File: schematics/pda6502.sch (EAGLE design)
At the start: 25 parts, among them IC1 74HC00D, IC2 74HC138D, IC3 DS1813-SMD, U1 W65C02S, U2 W65C22S, U3 28C256, U4 UM61256AK-12

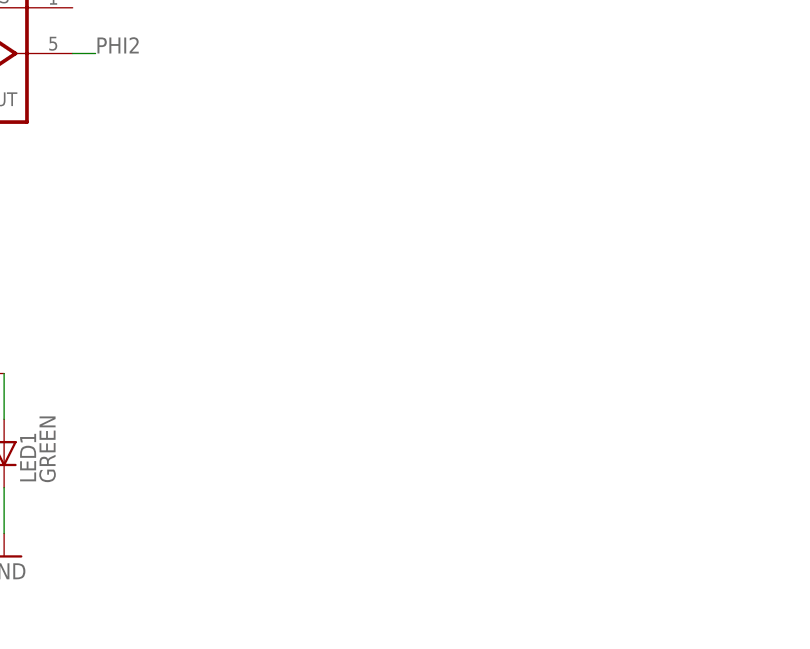
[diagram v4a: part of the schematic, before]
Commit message: schematics: VIA exposes two 2x7 headers; port A and port B.
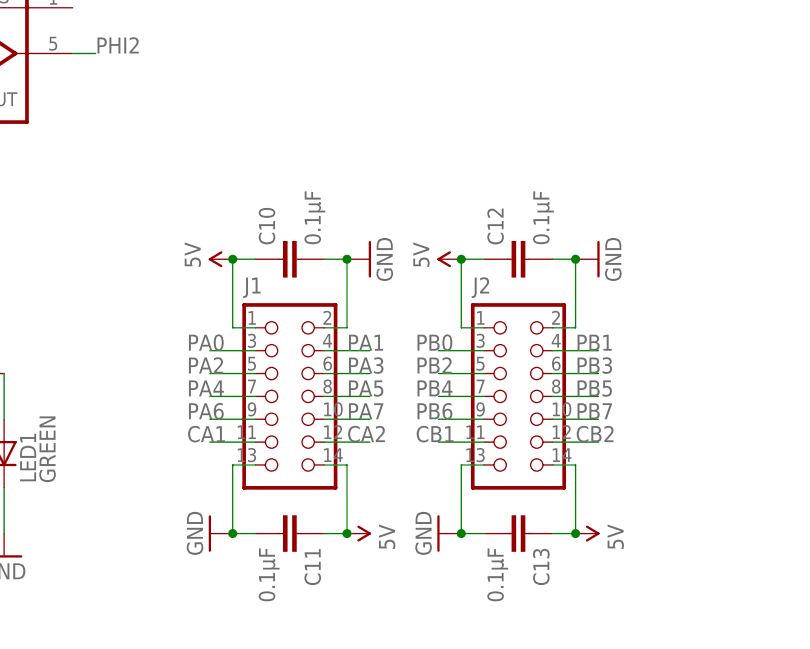
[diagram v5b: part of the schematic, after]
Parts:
- added C10, C11, C12, C13: 0.1μF, rcl:C-EUC0805
- added J1, J2: CON_HEADER_2X07-PTH, dangerousprototypes_devices:CON_HEADER_2X07-PTH
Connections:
- net 5V: now also C10.1, C11.1, C12.1, C13.1, J1.1, J1.14, J2.1, J2.14
- net CA1: now also J1.11
- net CA2: now also J1.12
- net CB1: now also J2.11
- net CB2: now also J2.12
- net GND: now also C10.2, C11.2, C12.2, C13.2, J1.13, J1.2, J2.13, J2.2
- net PA0: now also J1.3
- net PA1: now also J1.4
- net PA2: now also J1.5
- net PA3: now also J1.6
- net PA4: now also J1.7
- net PA5: now also J1.8
- net PA6: now also J1.9
- net PA7: now also J1.10
- net PB0: now also J2.3
- net PB1: now also J2.4
- net PB2: now also J2.5
- net PB3: now also J2.6
- net PB4: now also J2.7
- net PB5: now also J2.8
- net PB6: now also J2.9
- net PB7: now also J2.10

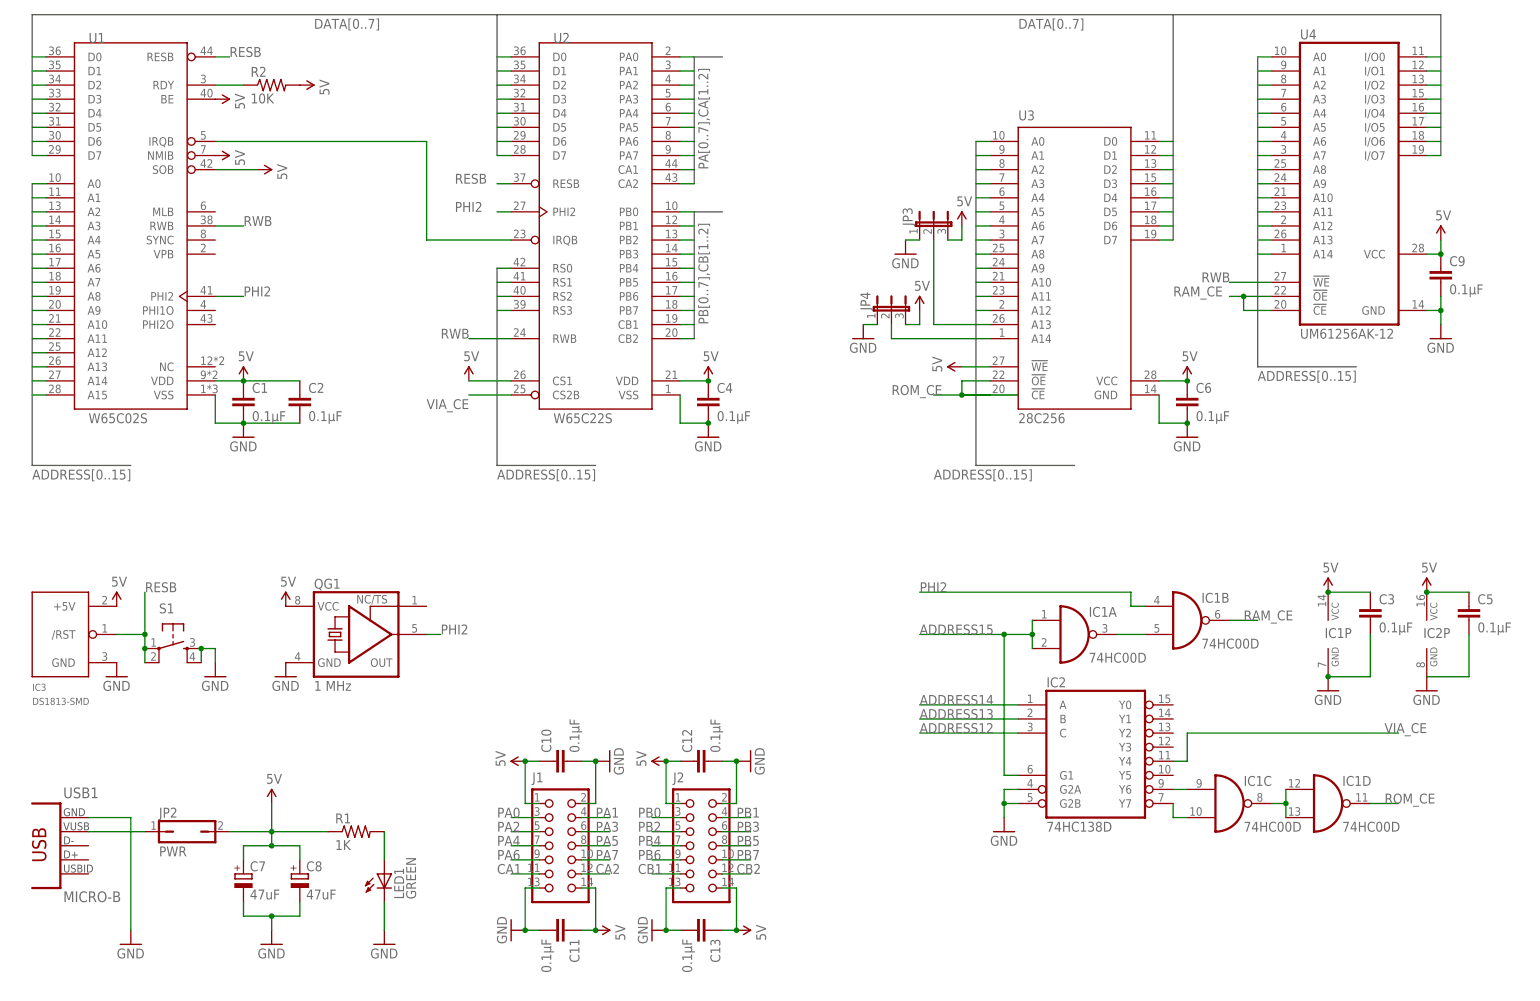
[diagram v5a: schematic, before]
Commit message: schematics: layout tweaks and errors corrected in schematic.
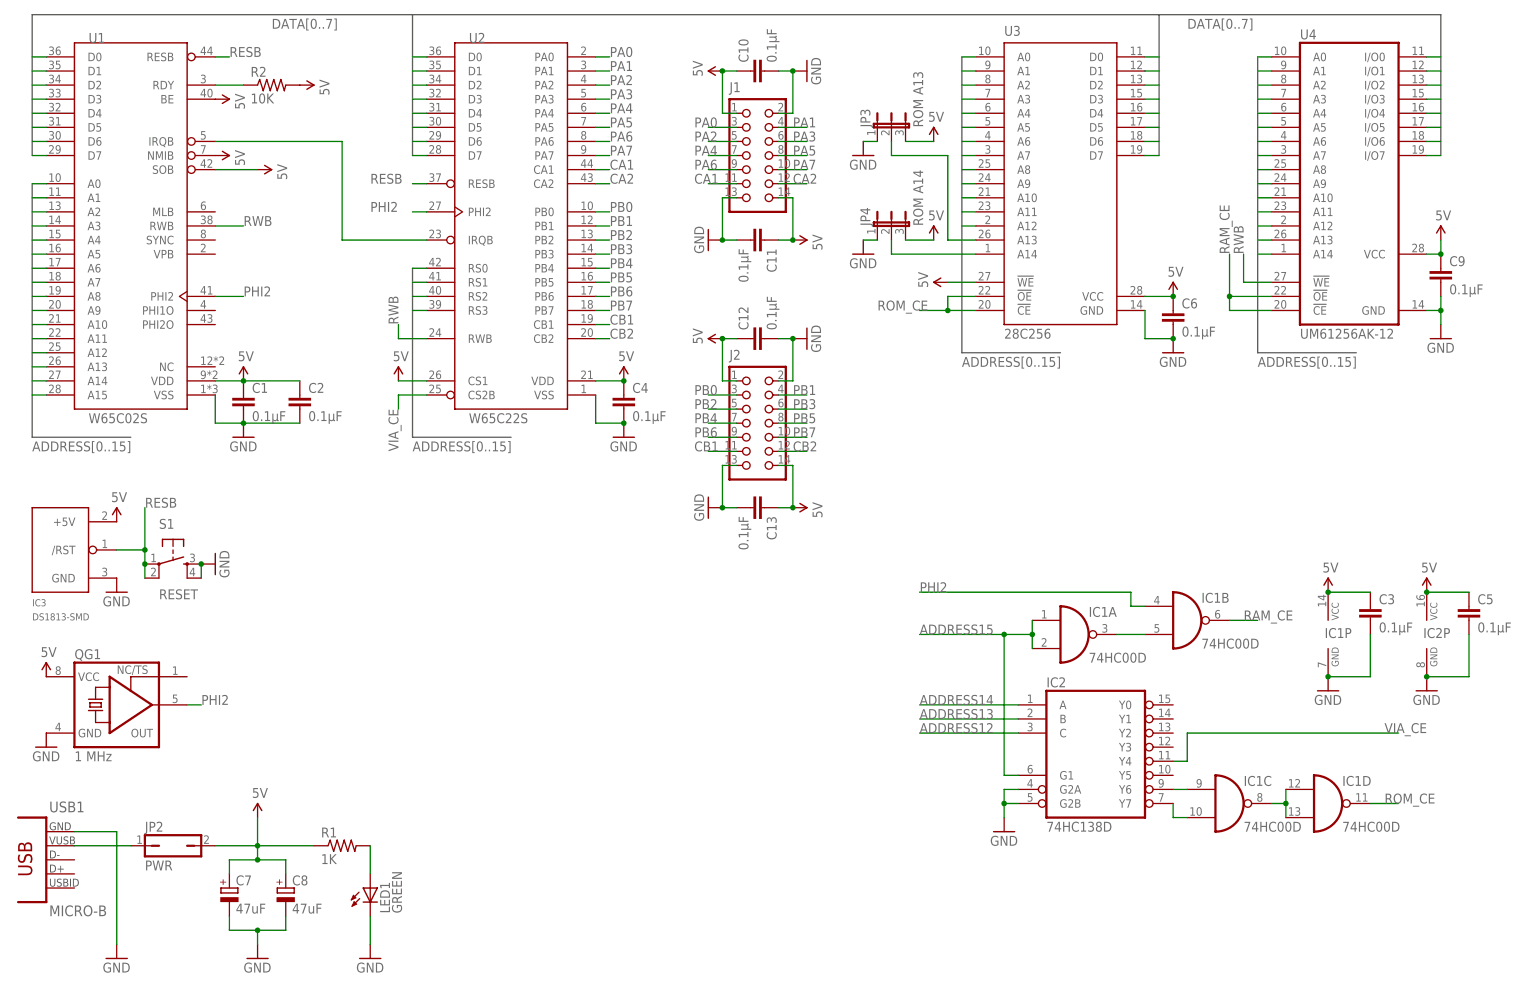
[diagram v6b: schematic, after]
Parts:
- JP3: value (none) -> ROM A13
- JP4: value (none) -> ROM A14
- S1: value (none) -> RESET
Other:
- moved on the sheet: C10, C11, C12, C13, C4, C6, C7, C8, IC3, J1, J2, JP2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

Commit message: schematics: TFT+SD header, plus schematic layout changes.
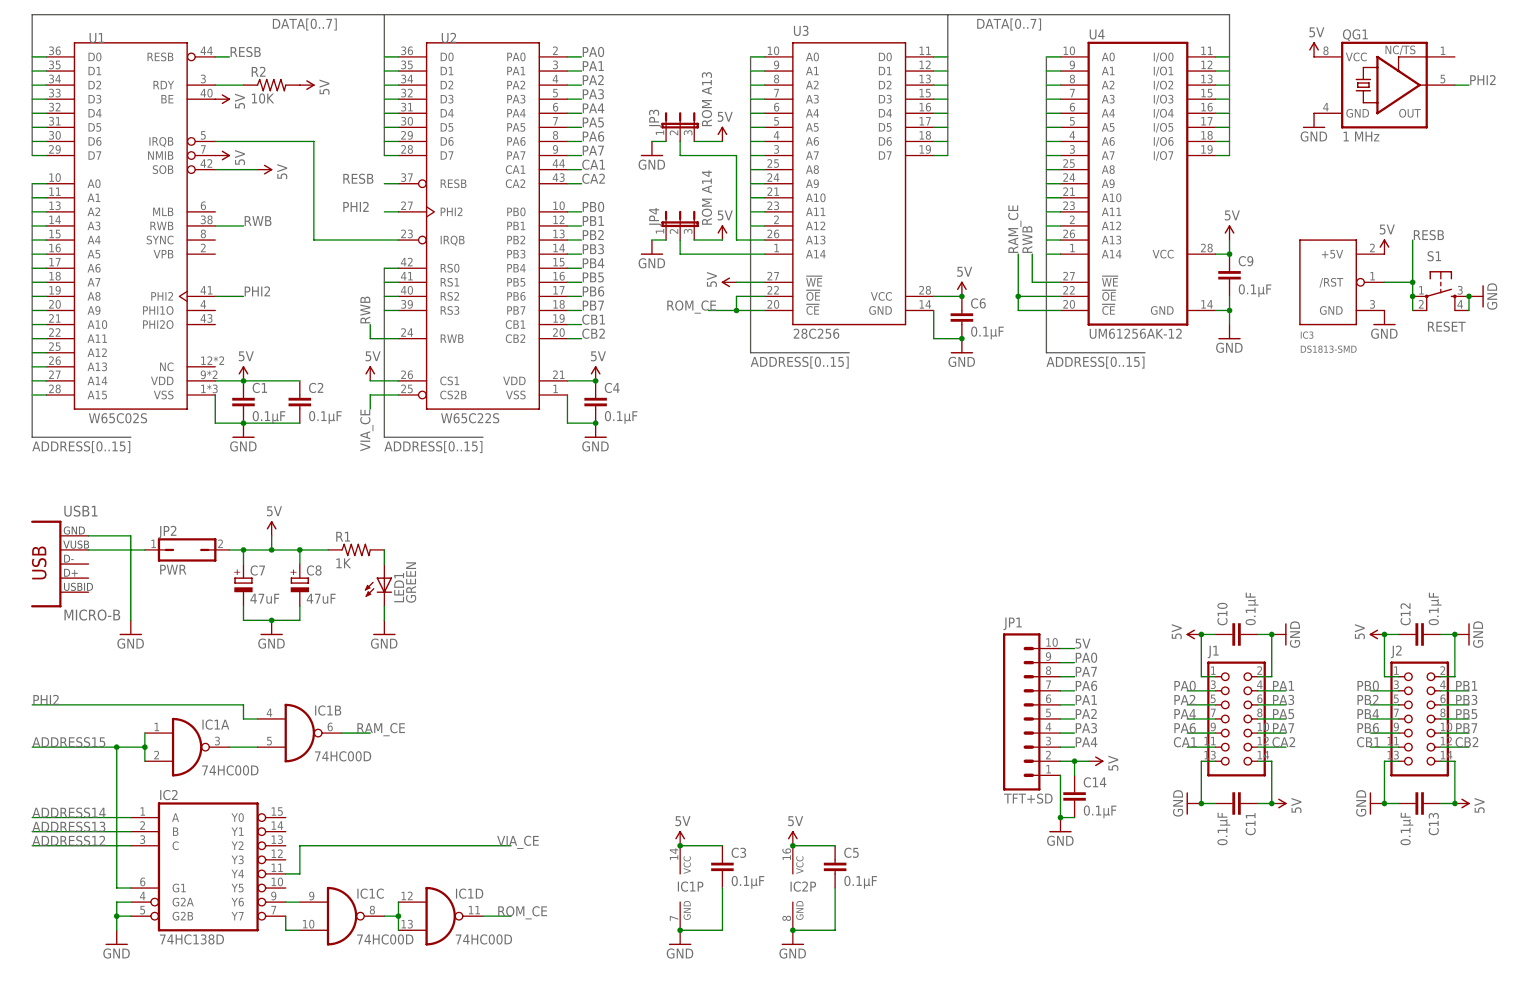
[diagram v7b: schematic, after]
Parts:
- added C14: 0.1μF, rcl:C-EUC0805
- added JP1: TFT+SD, SparkFun-Connectors:M10"
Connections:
- net 5V: now also C14.1, JP1.10, JP1.2
- net GND: now also C14.2, JP1.1
- net PA0: now also JP1.9
- net PA1: now also JP1.6
- net PA2: now also JP1.5
- net PA3: now also JP1.4
- net PA4: now also JP1.3
- net PA6: now also JP1.7
- net PA7: now also JP1.8
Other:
- moved on the sheet: C10, C11, C12, C13, C3, C4, C5, C6, C7, C8, C9, IC1A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

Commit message: schematics: renumbered parts (auto).
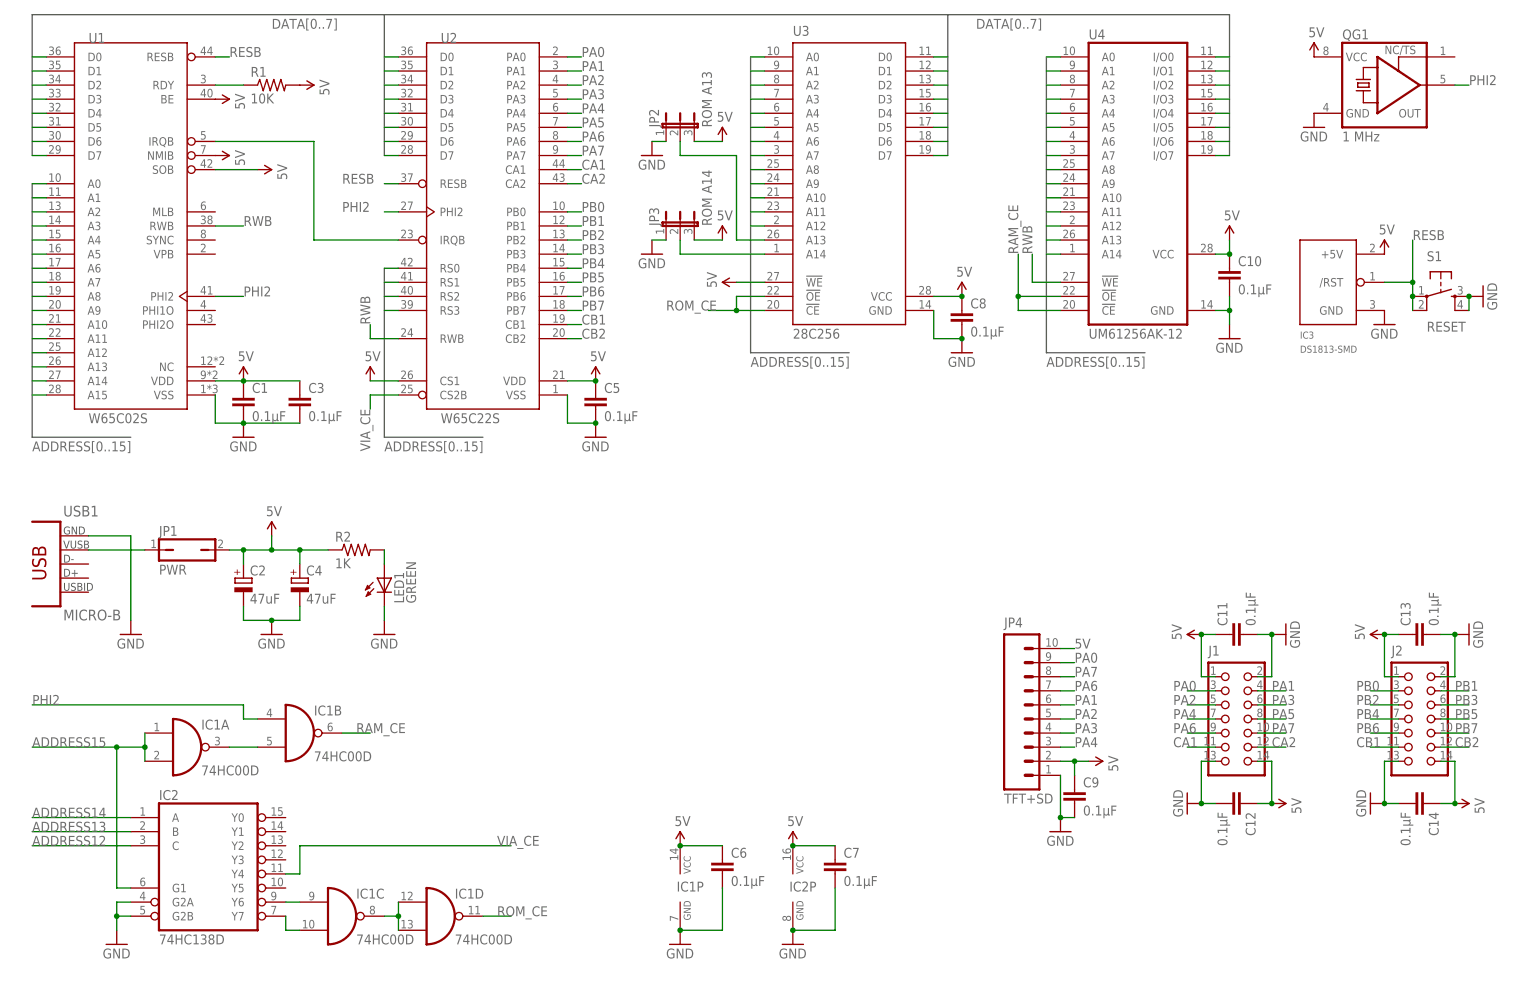
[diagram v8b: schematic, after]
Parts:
- C2, C4: value 0.1μF -> 47uF; device rcl:C-EUC0805 -> dangerousprototypes_devices:CAPACITOR_POL-CASE_B
- C7, C8: value 47uF -> 0.1μF; device dangerousprototypes_devices:CAPACITOR_POL-CASE_B -> rcl:C-EUC0805
- JP1: value TFT+SD -> PWR; device SparkFun-Connectors:M10" -> jumper:JP1Q
- JP2: value PWR -> ROM A13; device jumper:JP1Q -> jumper:JP2E
- JP3: value ROM A13 -> ROM A14
- JP4: value ROM A14 -> TFT+SD; device jumper:JP2E -> SparkFun-Connectors:M10"
- R1: value 1K -> 10K
- R2: value 10K -> 1K
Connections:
- net 5V: now also C2.+, C4.+, C7.1, C8.1, JP2.3, JP4.10, JP4.2, R1.2, R2.1; no longer C2.1, C4.1, C7.+, C8.+, JP1.10, JP2.2, JP4.3, R1.1, R2.2
- net GND: now also C2.-, C4.-, C7.2, C8.2, JP2.1; no longer C2.2, C4.2, C7.-, C8.-, JP1.1
- net N$1: now also R2.2; no longer R1.2
- net N$10: now also JP2.2; no longer JP3.2
- net N$4: now also JP1.1; no longer JP2.1
- net N$6: now also JP3.2; no longer JP4.2
- net N$9: now also R1.1; no longer R2.1
- net PA0: now also JP4.9; no longer JP1.9
- net PA1: now also JP4.6; no longer JP1.6
- net PA2: now also JP4.5; no longer JP1.5
- net PA3: now also JP4.4; no longer JP1.4
- net PA4: now also JP4.3; no longer JP1.3
- net PA6: now also JP4.7; no longer JP1.7
- net PA7: now also JP4.8; no longer JP1.8
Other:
- moved on the sheet: C10, C11, C12, C13, C14, C3, C5, C6, C9, JP3, R1, R2
